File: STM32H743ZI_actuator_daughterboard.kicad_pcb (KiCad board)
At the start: 2 copper layers, 300.8 x 186.2 mm, 202 parts, among them J1 Conn_01x02, J11 Picoblade, J13 Picoblade, J15 Picoblade, J17 Picoblade, J18 Conn_01x04, J19 Conn_02x10_Odd_Even, J2 Picoblade, J20 Conn_02x08_Odd_Even, J21 Conn_02x17_Odd_Even, J22 Conn_02x15_Odd_Even, J5 Picoblade, J7 Picoblade, J9 Picoblade, U1 DAC80508, U10 TLV3202AIDGKR, U11 OPA197xDBV, U12 DRV8837, U13 INA181A3IDBVR, U14 TLV3202AIDGKR, U15 OPA197xDBV, U16 DRV8837, U17 INA181A3IDBVR, U18 TLV3202AIDGKR, U19 OPA197xDBV, U2 REF5030AD, U20 DRV8837, U21 INA181A3IDBVR, U22 TLV3202AIDGKR, U23 OPA197xDBV, U24 DRV8837, U25 INA181A3IDBVR, U26 TLV3202AIDGKR, U27 OPA197xDBV, U28 DRV8837, U29 INA181A3IDBVR, U3 OPA197xDBV, U30 TLV3202AIDGKR, U31 OPA197xDBV, U32 DRV8837, U33 INA181A3IDBVR, U34 TLV3202AIDGKR, U35 OPA197xDBV, U36 OPA197xDBV, U37 OPA197xDBV, U38 XC6206PxxxMR, U4 TLV3202AIDGKR, U5 DRV8837, U6 OPA197xDBV, U7 INA181A3IDBVR, U8 DRV8837, U9 INA181A3IDBVR

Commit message: Working on how to arrange 8 channels
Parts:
- added REF**: NUCLEO-H743ZI, gabe_connectors:NUCLEO-H743ZI, F.Cu at (54.8, 121.8)
- C69, C70: footprint Capacitor_SMD:C_0402_1005Metric -> Capacitor_SMD:C_0603_1608Metric
- moved U2 80.0 mm to (27.5, 88.7)
- moved C3 78.9 mm to (22.9, 89.4), turned to -90 degrees
- moved C58 76.4 mm to (43.5, 92.7), turned to 0 degrees
- moved J17 76.1 mm to (37.9, 95.0), turned to 90 degrees
- moved R42 75.6 mm to (40.8, 94.1), turned to -90 degrees
- moved C57 75.0 mm to (46.6, 92.7), turned to 0 degrees
- moved C5 73.1 mm to (29.7, 92.4), turned to 180 degrees
- moved U32 72.5 mm to (43.6, 94.8), turned to 0 degrees
- moved J18 71.6 mm to (42.9, 86.0), turned to 90 degrees
- moved C4 70.7 mm to (32.1, 89.9), turned to -90 degrees
- moved U34 69.2 mm to (48.4, 95.3), turned to 180 degrees
- moved R39 67.8 mm to (52.3, 95.5), turned to -90 degrees
- moved U33 67.4 mm to (41.7, 98.1), turned to 180 degrees
- moved C63 64.9 mm to (46.7, 97.8), turned to 0 degrees
- moved C62 63.5 mm to (40.8, 100.6), turned to 0 degrees
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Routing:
- net GND: vias 324 -> 306
- net /PWM_controller_4/Isense: vias 0 -> 9
- net /PWM_controller_8/Isense: vias 0 -> 9
- net /PWM_controller_7/Isense: vias 0 -> 9
- net /PWM_controller_2/Isense: vias 0 -> 9
- net /PWM_controller_6/Isense: vias 0 -> 9
- net /PWM_controller_3/Isense: vias 0 -> 9
- net Vmotor: vias 54 -> 18
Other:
- board size 300.8 x 186.2 mm -> 70.6 x 83.3 mm

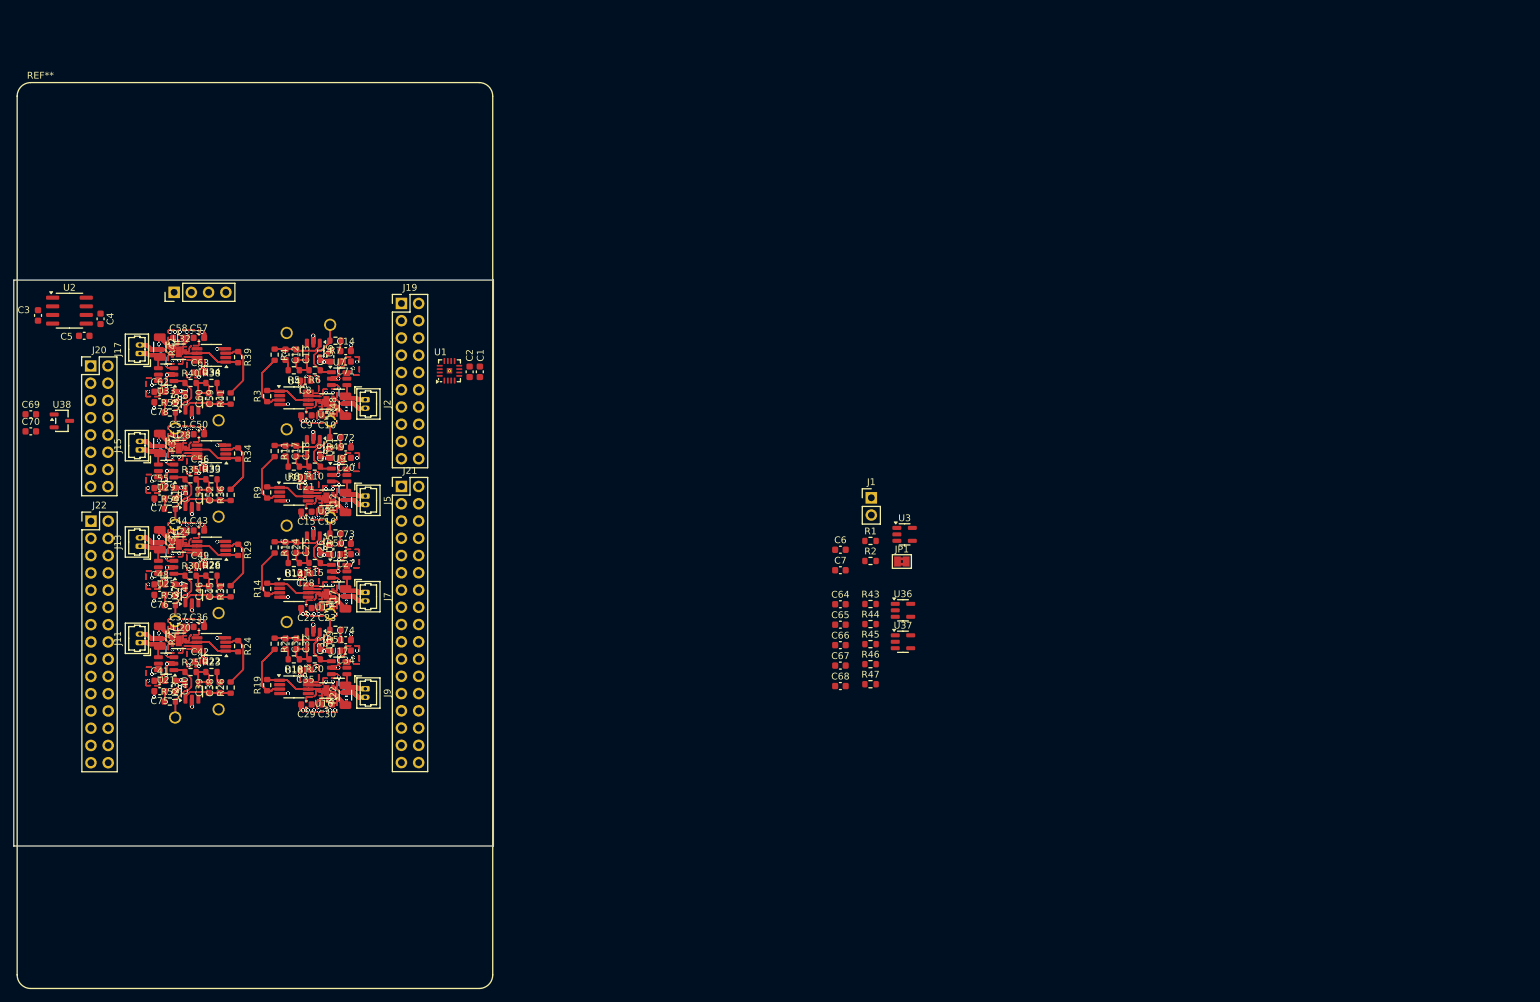
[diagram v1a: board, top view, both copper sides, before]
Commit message: Continuing layout, added ADC connections for current measurements
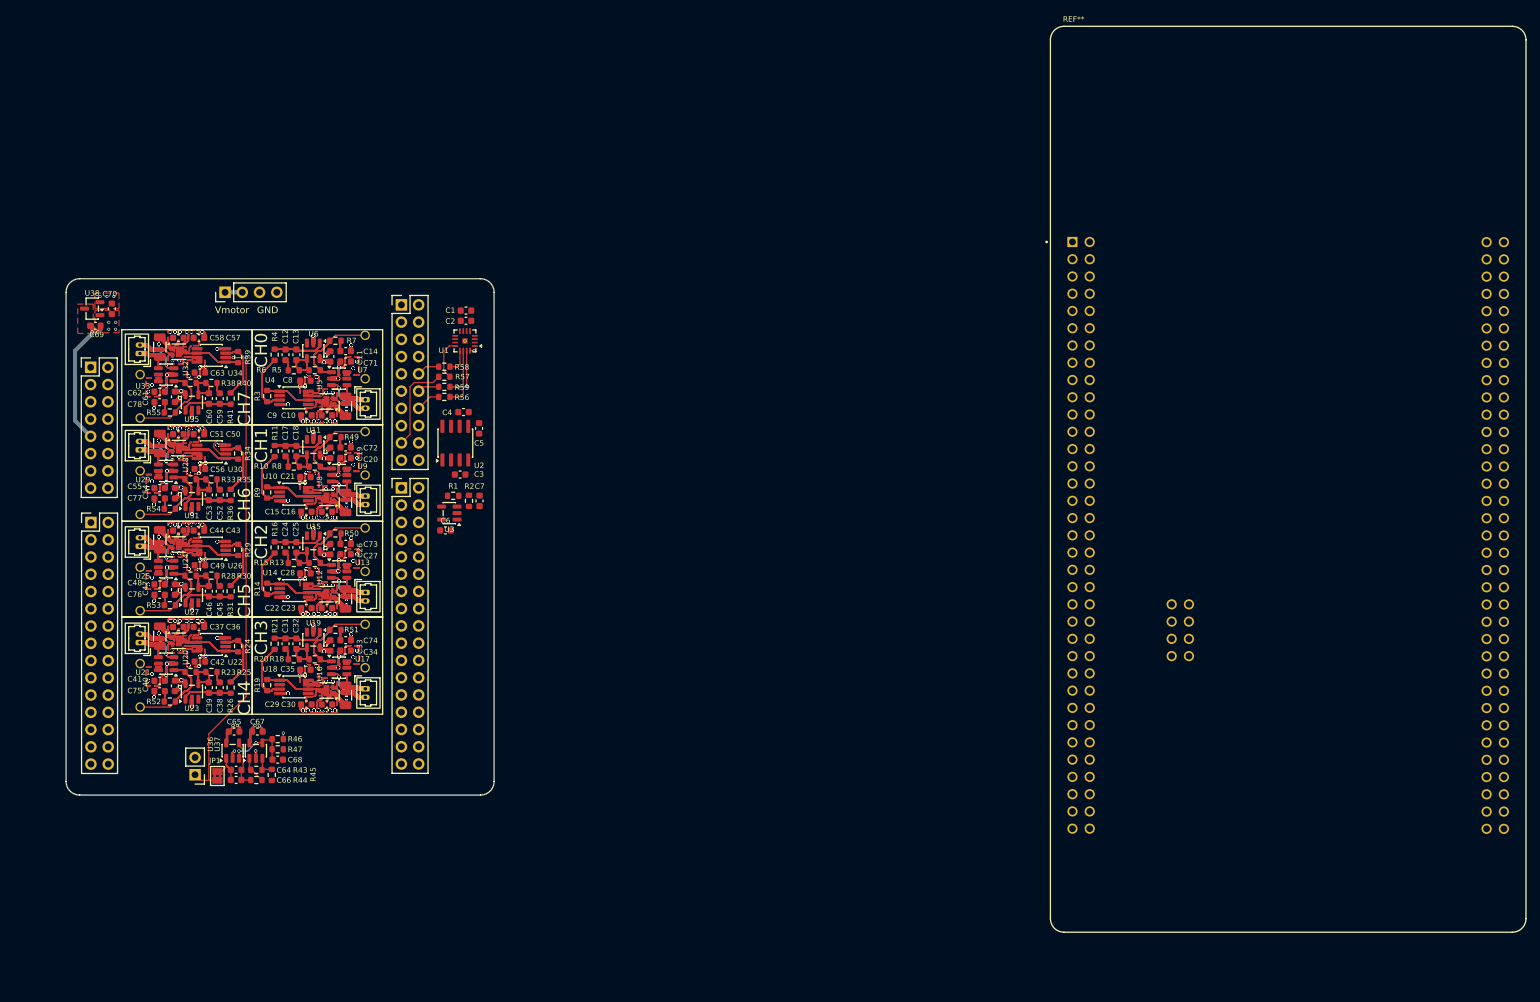
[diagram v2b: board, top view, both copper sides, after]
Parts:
- added R56: 22, Resistor_SMD:R_0603_1608Metric, F.Cu at (82.7, 101.4)
- added R57: 22, Resistor_SMD:R_0603_1608Metric, F.Cu at (82.7, 98.4)
- added R58: 22, Resistor_SMD:R_0603_1608Metric, F.Cu at (82.7, 97.0)
- added R59: 22, Resistor_SMD:R_0603_1608Metric, F.Cu at (82.7, 99.9)
- moved REF** 152.3 mm to (206.9, 113.5)
- moved J1 107.6 mm to (46.0, 157.0), turned to 180 degrees
- moved JP1 105.6 mm to (49.3, 157.2), turned to 90 degrees
- moved U36 100.8 mm to (51.5, 153.5), turned to 90 degrees
- moved U37 96.6 mm to (54.9, 153.5), turned to 90 degrees
- moved R43 93.6 mm to (55.0, 156.3)
- moved R44 93.3 mm to (55.0, 157.8)
- moved C64 92.2 mm to (52.0, 156.3)
- moved C66 91.1 mm to (52.0, 157.8)
- moved C65 90.6 mm to (51.7, 150.7)
- moved R45 90.2 mm to (57.3, 157.0), turned to -90 degrees
- moved R46 87.9 mm to (58.2, 151.8)
- moved R47 87.8 mm to (58.2, 153.3), turned to 180 degrees
- moved C67 86.4 mm to (55.2, 150.6)
- moved C68 83.5 mm to (58.2, 154.8)
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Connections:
- C14 pad 1: /PWM_controller_1/Isense_out -> /ADC3_IN4
- C72 pad 1: /PWM_controller_2/Isense_out -> /ADC3_IN5
- C73 pad 1: /PWM_controller_3/Isense_out -> /ADC3_IN2
- C74 pad 1: /PWM_controller_4/Isense_out -> /ADC3_IN3
- C75 pad 1: /PWM_controller_5/Isense_out -> /ADC3_IN7
- C76 pad 1: /PWM_controller_6/Isense_out -> /ADC3_IN6
- C77 pad 1: /PWM_controller_7/Isense_out -> /ADC3_IN0
- C78 pad 1: /PWM_controller_8/Isense_out -> /ADC3_IN1
- J19 pad 17: unconnected-(J19-Pin_17-Pad17) -> /Connectors/SPI1_nCS
- J19 pad 20: unconnected-(J19-Pin_20-Pad20) -> /ADC3_IN5
- J19 pad 9: /Connectors/SPI1_nCS -> unconnected-(J19-Pin_9-Pad9)
- J20 pad 11: unconnected-(J20-Pin_11-Pad11) -> GND
- J20 pad 13: unconnected-(J20-Pin_13-Pad13) -> GND
- J21 pad 9: unconnected-(J21-Pin_9-Pad9) -> /ADC3_IN4
- J22 pad 11: unconnected-(J22-Pin_11-Pad11) -> /ADC3_IN6
- J22 pad 24: unconnected-(J22-Pin_24-Pad24) -> /ADC3_IN7
- J22 pad 26: unconnected-(J22-Pin_26-Pad26) -> /ADC3_IN3
- J22 pad 28: unconnected-(J22-Pin_28-Pad28) -> /ADC3_IN2
- J22 pad 5: unconnected-(J22-Pin_5-Pad5) -> /ADC3_IN1
- J22 pad 9: unconnected-(J22-Pin_9-Pad9) -> /ADC3_IN0
- R49 pad 1: /PWM_controller_2/Isense_out -> /ADC3_IN5
- R50 pad 1: /PWM_controller_3/Isense_out -> /ADC3_IN2
- R51 pad 1: /PWM_controller_4/Isense_out -> /ADC3_IN3
- R52 pad 1: /PWM_controller_5/Isense_out -> /ADC3_IN7
- R53 pad 1: /PWM_controller_6/Isense_out -> /ADC3_IN6
- R54 pad 1: /PWM_controller_7/Isense_out -> /ADC3_IN0
- R55 pad 1: /PWM_controller_8/Isense_out -> /ADC3_IN1
- R7 pad 1: /PWM_controller_1/Isense_out -> /ADC3_IN4
- U1 pad 12: /Connectors/SPI1_nCS -> Net-(U1-~{CS})
- U1 pad 13: /Connectors/SPI1_SCK -> Net-(U1-SCLK)
- U1 pad 14: /Connectors/SPI1_MOSI -> Net-(U1-SDI)
- U1 pad 15: /Connectors/SPI1_MISO -> Net-(U1-SDO/~{ALARM})
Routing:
- net GND: track 263.7 -> 474.2 mm, vias 306 -> 581
- net /Triangle: track 0.00 -> 74.9 mm, vias 0 -> 2
- net +3V3: track 47.0 -> 90.9 mm, vias 216 -> 395
- net /PWM_controller_6/FRA_2: track 27.4 -> 54.7 mm
- net /PWM_controller_5/FRA_2: track 27.4 -> 54.7 mm
- net /PWM_controller_3/FRA_2: track 27.4 -> 54.7 mm
- net /PWM_controller_2/FRA_2: track 27.4 -> 54.7 mm
- net /PWM_controller_4/FRA_2: track 54.7 -> 82.1 mm
- net /PWM_controller_1/FRA_2: track 27.4 -> 54.7 mm
- net /PWM_controller_7/FRA_2: track 27.4 -> 54.7 mm
- net /PWM_controller_5/OUT1: track 26.4 -> 52.7 mm, vias 6 -> 12
- net /PWM_controller_6/OUT1: track 26.4 -> 52.7 mm, vias 6 -> 12
- net /PWM_controller_4/OUT1: track 52.7 -> 79.1 mm, vias 12 -> 18
- net /PWM_controller_7/OUT1: track 26.4 -> 52.7 mm, vias 6 -> 12
- net /PWM_controller_2/OUT1: track 26.4 -> 52.7 mm, vias 6 -> 12
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- added copper zone on In2.Cu, net +3V3
- added copper zone on F.Cu, net +5V
- added copper zone on In1.Cu, net GND
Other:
- board size 70.6 x 83.3 mm -> 63 x 76 mm
- copper layers 2 -> 4
- board text added: "CH0"
- board text added: "CH1"
- board text added: "CH2"
- board text added: "CH3"
- board text added: "CH4"
- board text added: "CH5"
- board text added: "CH6"
- board text added: "CH7"
- board text added: "GND"
- board text added: "Vmotor"

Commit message: Basically Done with Layout, final checks and let it sit a day before ordering
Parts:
- removed REF**: NUCLEO-H743ZI, gabe_connectors:NUCLEO-H743ZI
- added C79: 100n, Capacitor_SMD:C_0603_1608Metric, F.Cu at (87.0, 97.0)
- moved R57 1.51 mm to (82.7, 96.9)
- moved R58 1.47 mm to (82.7, 98.4)
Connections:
- C14 pad 1: /ADC3_IN4 -> /ADC3_IN5
- C72 pad 1: /ADC3_IN5 -> /ADC3_IN4
- R49 pad 1: /ADC3_IN5 -> /ADC3_IN4
- R7 pad 1: /ADC3_IN4 -> /ADC3_IN5
- U2 pad 3: /TEMP_OUT -> unconnected-(U2-Temp-Pad3)
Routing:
- net GND: track 474.2 -> 99.5 mm, vias 581 -> 159
- net Vsplit: track 0.00 -> 293.6 mm, vias 0 -> 17
- net Vmotor: track 2.54 -> 166.4 mm, vias 96 -> 23
- net /PWM_controller_5/Vset: track 0.00 -> 105.2 mm, vias 0 -> 2
- net /PWM_controller_6/Vset: track 0.00 -> 77.7 mm, vias 0 -> 4
- net /PWM_controller_4/FRA_2: track 82.1 -> 9.12 mm
- net /PWM_controller_4/Vset: track 0.00 -> 71.6 mm, vias 0 -> 2
- net /PWM_controller_4/OUT1: track 79.1 -> 8.79 mm, vias 18 -> 2
- net /PWM_controller_4/Vcomp+: track 75.2 -> 8.36 mm
- net /PWM_controller_7/Vset: track 0.00 -> 64.1 mm, vias 0 -> 4
- net +3V3: track 90.9 -> 26.9 mm, vias 395 -> 75
- net /PWM_controller_4/Isense: track 74.8 -> 13.2 mm
- net /PWM_controller_4/FRA_1: track 67.0 -> 7.45 mm
- net /PWM_controller_3/Vset: track 0.00 -> 58.7 mm, vias 0 -> 2
- net /ADC3_IN2: track 9.38 -> 66.5 mm, vias 0 -> 3
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- added copper zone on B.Cu, net GND
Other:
- board text added: "MISO"
- board text added: "MOSI"
- board text added: "SCK"
- board text added: "Triangle"
- board text added: "~{CS}"
